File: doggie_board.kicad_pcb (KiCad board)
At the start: 2 copper layers, 127 x 127.5 mm, 86 parts, among them J1 XT90PW-M, J2 XT90PW-M, J5V1 Conn_01x02, J5V10 Conn_01x02, J5V11 Conn_01x02, J5V12 Conn_01x02, J5V13 Conn_01x02, J5V14 Conn_01x02, J5V15 Conn_01x02, J5V16 Conn_01x02, J5V17 Conn_01x02, J5V18 Conn_01x02, J5V19 Conn_01x02, J5V2 Conn_01x02, J5V20 Conn_01x02, J5V3 Conn_01x02, J5V4 Conn_01x02, J5V5 Conn_01x02, J5V6 Conn_01x02, J5V7 Conn_01x02, J5V8 Conn_01x02, J5V9 Conn_01x02, Q1 PSMN3R7-100BSEJ, Q2 PSMN3R7-100BSEJ, Q3 PSMN3R7-100BSEJ, Q4 PSMN3R7-100BSEJ, Q5 PSMN3R7-100BSEJ, Q6 PSMN3R7-100BSEJ, U1 TPS2490, U2 TPS2490, U3 LM76005, U4 LM76005, U5 LM76005

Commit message: progress on right drain
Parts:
- moved R5 9.63 mm to (127.1, 71.1), turned to -90 degrees
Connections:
- Q1 pad 2: (no net) -> /High Side Power Switch/drain_left
- Q2 pad 2: (no net) -> /High Side Power Switch/drain_left
- Q3 pad 2: (no net) -> /High Side Power Switch/drain_left
- Q4 pad 2: (no net) -> /High Side Power Switch/drain_r
- Q5 pad 2: (no net) -> /High Side Power Switch/drain_r
- Q6 pad 2: (no net) -> /High Side Power Switch/drain_r
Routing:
- net (no net): vias 1 -> 0
- added copper zone on F.Cu, net /High Side Power Switch/drain_left
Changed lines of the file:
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@@
 			(layers "F.Cu" "F.Mask")
 			(roundrect_rratio 0.026596)
+			(net 53 "/High Side Power Switch/drain_r")
+			(pintype "passive")
 		)
 		(pad "3" smd roundrect
@@
 			(layers "F.Cu" "F.Mask")
 			(roundrect_rratio 0.026596)
+			(net 53 "/High Side Power Switch/drain_r")
+			(pintype "passive")
 		)
 		(pad "3" smd roundrect
@@
 			(layers "F.Cu" "F.Mask")
 			(roundrect_rratio 0.026596)
+			(net 53 "/High Side Power Switch/drain_r")
+			(pintype "passive")
 		)
 		(pad "3" smd roundrect
@@
 			(layers "F.Cu" "F.Mask")
 			(roundrect_rratio 0.026596)
+			(net 51 "/High Side Power Switch/drain_left")
+			(pintype "passive")
 		)
 		(pad "3" smd roundrect
@@
 	(footprint "footprints:RES_PSR500_ROM"
 		(layer "F.Cu")
-		(at 130.25 62 180)
+		(at 127.1 71.1 -90)
 		(tags "PSR500HTQFC0L20 ")
 		(property "Reference" "R5"
-			(at 0 0 180)
+			(at 0 0 270)
 			(unlocked yes)
 			(layer "F.SilkS")
@@
 		)
 		(property "Value" "0.2m, 15W"
-			(at 0 0 180)
+			(at 0 0 270)
 			(unlocked yes)
 			(layer "F.Fab")
@@
 		)
 		(property "Datasheet" "~"
-			(at 0 0 180)
+			(at 0 0 90)
 			(layer "F.Fab")
 			(hide yes)
@@
 		)
 		(property "Description" "Resistor"
-			(at 0 0 180)
+			(at 0 0 90)
 			(layer "F.Fab")
 			(hide yes)
@@
 		)
 		(property "Sim.Device" ""
-			(at 0 0 180)
+			(at 0 0 270)
 			(unlocked yes)
 			(layer "F.Fab")
@@
 		)
 		(property "Sim.Pins" ""
-			(at 0 0 180)
+			(at 0 0 270)
 			(unlocked yes)
 			(layer "F.Fab")
@@
 		)
 		(property "Sim.Type" ""
-			(at 0 0 180)
+			(at 0 0 270)
 			(unlocked yes)
 			(layer "F.Fab")
@@
 		(attr smd)
 		(fp_line
-			(start 2.74045 -4.1529)
-			(end -2.74045 -4.1529)
+			(start -2.74045 4.1529)
+			(end 2.74045 4.1529)
 			(stroke
 				(width 0.1524)
@@
 		)
 		(fp_line
-			(start -2.74045 4.1529)
-			(end 2.74045 4.1529)
+			(start 2.74045 -4.1529)
+			(end -2.74045 -4.1529)
 			(stroke
 				(width 0.1524)
@@
 		)
 		(fp_line
-			(start 8.1026 4.2799)
-			(end -8.1026 4.2799)
+			(start -8.1026 4.2799)
+			(end -8.1026 -4.2799)
 			(stroke
 				(width 0.1524)
@@
 		)
 		(fp_line
-			(start 8.1026 -4.2799)
-			(end 8.1026 4.2799)
+			(start 8.1026 4.2799)
+			(end -8.1026 4.2799)
 			(stroke
 				(width 0.1524)
@@
 		)
 		(fp_line
-			(start -8.1026 4.2799)
-			(end -8.1026 -4.2799)
+			(start -8.1026 -4.2799)
+			(end 8.1026 -4.2799)
 			(stroke
 				(width 0.1524)
@@
 		)
 		(fp_line
-			(start -8.1026 -4.2799)
-			(end 8.1026 -4.2799)
+			(start 8.1026 -4.2799)
+			(end 8.1026 4.2799)
 			(stroke
 				(width 0.1524)
@@
 		)
 		(fp_line
-			(start 7.6454 4.0259)
-			(end 7.6454 -4.0259)
+			(start -7.6454 4.0259)
+			(end -3.048 4.0259)
 			(stroke
 				(width 0.0254)
@@
 		)
 		(fp_line
-			(start 7.6454 4.0259)
-			(end 7.6454 -4.0259)
+			(start -7.6454 4.0259)
+			(end 7.6454 4.0259)
 			(stroke
 				(width 0.0254)
@@
 		)
 		(fp_line
-			(start 7.6454 -4.0259)
-			(end 3.048 -4.0259)
+			(start -3.048 4.0259)
+			(end -3.048 -4.0259)
 			(stroke
 				(width 0.0254)
@@
 		)
 		(fp_line
-			(start 7.6454 -4.0259)
-			(end -7.6454 -4.0259)
+			(start 3.048 4.0259)
+			(end 7.6454 4.0259)
 			(stroke
 				(width 0.0254)
@@
 		)
 		(fp_line
-			(start 3.048 4.0259)
-			(end 7.6454 4.0259)
+			(start 7.6454 4.0259)
+			(end 7.6454 -4.0259)
 			(stroke
 				(width 0.0254)
@@
 		)
 		(fp_line
-			(start 3.048 -4.0259)
-			(end 3.048 4.0259)
+			(start 7.6454 4.0259)
+			(end 7.6454 -4.0259)
 			(stroke
 				(width 0.0254)
@@
 		)
 		(fp_line
-			(start -3.048 4.0259)
-			(end -3.048 -4.0259)
+			(start -7.6454 -4.0259)
+			(end -7.6454 4.0259)
 			(stroke
 				(width 0.0254)
@@
 		)
 		(fp_line
-			(start -3.048 -4.0259)
-			(end -7.6454 -4.0259)
+			(start -7.6454 -4.0259)
+			(end -7.6454 4.0259)
 			(stroke
 				(width 0.0254)
@@
 		)
 		(fp_line
-			(start -7.6454 4.0259)
-			(end 7.6454 4.0259)
+			(start -3.048 -4.0259)
+			(end -7.6454 -4.0259)
 			(stroke
 				(width 0.0254)
@@
 		)
 		(fp_line
-			(start -7.6454 4.0259)
-			(end -3.048 4.0259)
+			(start 3.048 -4.0259)
+			(end 3.048 4.0259)
 			(stroke
 				(width 0.0254)
@@
 		)
 		(fp_line
-			(start -7.6454 -4.0259)
-			(end -7.6454 4.0259)
+			(start 7.6454 -4.0259)
+			(end -7.6454 -4.0259)
 			(stroke
 				(width 0.0254)
@@
 		)
 		(fp_line
-			(start -7.6454 -4.0259)
-			(end -7.6454 4.0259)
+			(start 7.6454 -4.0259)
+			(end 3.048 -4.0259)
 			(stroke
 				(width 0.0254)
@@
 		)
 		(fp_text user "${REFERENCE}"
-			(at 0 0 180)
+			(at 0 0 270)
 			(unlocked yes)
 			(layer "F.Fab")
@@
 		)
 		(pad "1" smd rect
-			(at -5.4483 0 180)
+			(at -5.4483 0 270)
 			(size 4.8006 8.0518)
 			(layers "F.Cu" "F.Mask" "F.Paste")
@@
 		)
 		(pad "2" smd rect
-			(at 5.4483 0 180)
+			(at 5.4483 0 270)
 			(size 4.8006 8.0518)
 			(layers "F.Cu" "F.Mask" "F.Paste")
@@
 			(polygon
 				(pts
-					(xy 133.2472 65.9751) (xy 127.2528 65.9751) (xy 127.2528 58.0249) (xy 133.2472 58.0249)
+					(xy 131.0751 68.1028) (xy 131.0751 74.0972) (xy 123.1249 74.0972) (xy 123.1249 68.1028)
 				)
 			)
@@
 			(layers "F.Cu" "F.Mask")
 			(roundrect_rratio 0.026596)
+			(net 51 "/High Side Power Switch/drain_left")
+			(pintype "passive")
 		)
 		(pad "3" smd roundrect
@@
 			(layers "F.Cu" "F.Mask")
 			(roundrect_rratio 0.026596)
+			(net 51 "/High Side Power Switch/drain_left")
+			(pintype "passive")
 		)
 		(pad "3" smd roundrect
@@
 		(layer "Edge.Cuts")
 	)
-	(via
-		(at 131.4 126.45)
-		(size 1)
-		(drill 0.8)
-		(layers "F.Cu" "B.Cu")
-		(free yes)
-		(net 0)
-	)
 	(zone
 		(net 2)
@@
 			)
 		)
+	)
+	(zone
+		(net 51)
+		(net_name "/High Side Power Switch/drain_left")
+		(layer "F.Cu")
+		(hatch edge 0.5)
+		(priority 1)
+		(connect_pads
+			(clearance 0.5)
+		)
+		(min_thickness 0.25)
+		(filled_areas_thickness no)
+		(fill yes
+			(thermal_gap 0.5)
+			(thermal_bridge_width 0.5)
+		)
+		(polygon
+			(pts
+				(xy 120.2 71.7) (xy 119.8 162.7) (xy 133 162.7) (xy 133 71.7)
+			)
+		)

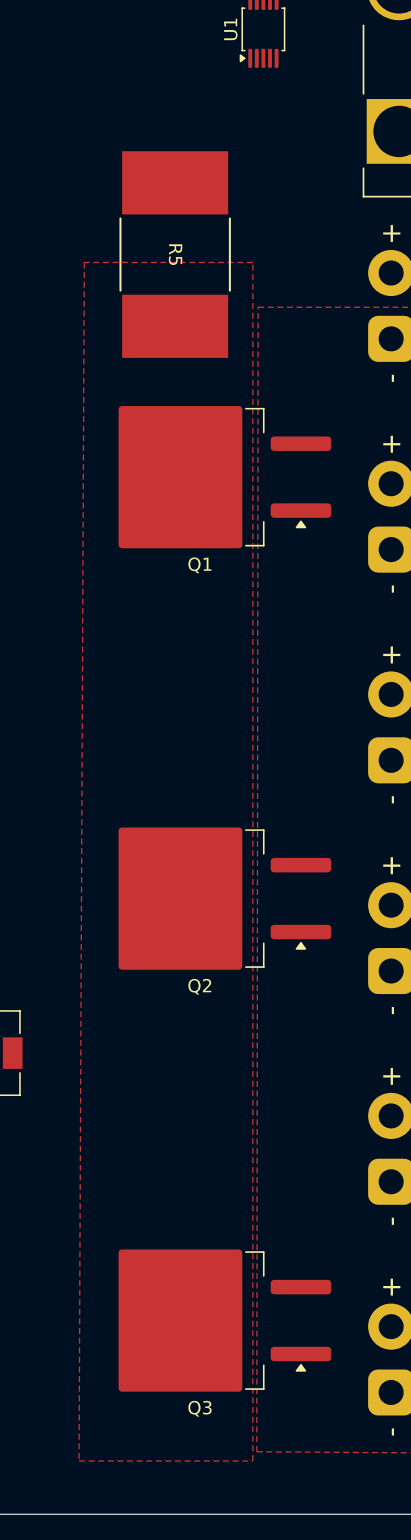
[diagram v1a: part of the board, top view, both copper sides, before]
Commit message: swapped left and right
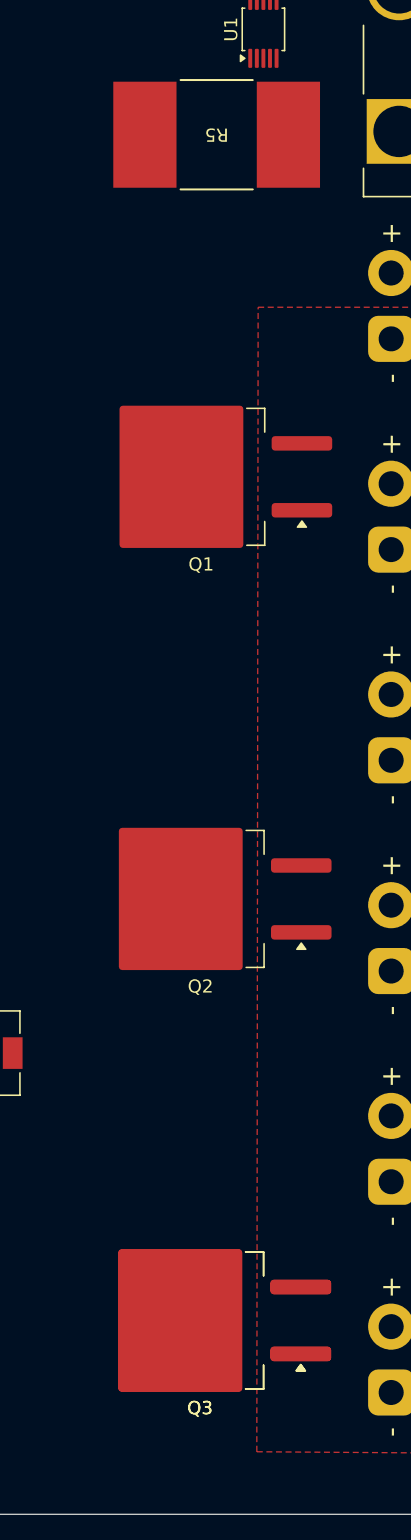
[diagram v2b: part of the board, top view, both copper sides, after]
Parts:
- added Q3: PSMN3R7-100BSEJ, Package_TO_SOT_SMD:TO-263-2, F.Cu at (129.0, 152.0)
- moved R5 9.63 mm to (130.2, 62.0), turned to 180 degrees
- moved Q1 0.08 mm to (129.1, 88.0)
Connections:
- Q3 pad 2: /High Side Power Switch/drain_left -> (no net)
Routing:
- removed copper zone on F.Cu, net /High Side Power Switch/drain_left

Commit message: Fixed Schematics with more cost effective IC's
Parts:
- removed the Q3 at (129.0, 152.0)
- added J3: Conn_01x02, Connector_PinHeader_2.54mm:PinHeader_1x02_P2.54mm_Vertical, F.Cu at (258.0, 124.5)
- C3: value 0.1uF, 100V -> 2.2uF
- C4: value 27nF, 100V -> 10nF
- R10: value 100k -> 50; footprint Resistor_SMD:R_0201_0603Metric_Pad0.64x0.40mm_HandSolder -> Resistor_SMD:R_1206_3216Metric_Pad1.30x1.75mm_HandSolder
- R11: value 18k -> 50; footprint Resistor_SMD:R_0201_0603Metric_Pad0.64x0.40mm_HandSolder -> Resistor_SMD:R_1206_3216Metric_Pad1.30x1.75mm_HandSolder
- R12: value 0.2m, 15W -> 50; footprint footprints:RES_PSR500_ROM -> Resistor_SMD:R_1206_3216Metric_Pad1.30x1.75mm_HandSolder
- R13: value 50 -> 200k
- R14: value 50 -> 100k
- R15: value 50 -> 560
- R16: value 1k -> 2.2
- U4: value LM76005 -> MIC28516T-E/PHA
- moved C1 86.6 mm to (135.0, 45.0), turned to 90 degrees
- moved R1 82.7 mm to (132.5, 60.0)
- moved R2 58.1 mm to (129.0, 60.0)
- moved U1 18.9 mm to (115.2, 57.1)
- moved R5 9.41 mm to (127.5, 71.0), turned to -90 degrees
- moved D1 2.92 mm to (127.0, 47.2), turned to 180 degrees
- moved J1 2.65 mm to (150.8, 56.3)
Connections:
- C1 pad 1: 48_L -> 48_RAW
- C3 pad 1: 48_R -> /12v Buck Converter/VDD
- C4 pad 1: Net-(C4-Pad1) -> /12v Buck Converter/BST
- C4 pad 2: GND -> Net-(C4-Pad2)
- Cboot2 pad 1: Net-(U4-BOOT) -> unconnected-(Cboot2-Pad1)
- Cin1 pad 1: +48V -> 48_R
- Cin2 pad 1: +48V -> 48_R
- Cinx1 pad 1: +48V -> 48_R
- Cinx2 pad 1: +48V -> 48_R
- Cinx3 pad 1: +48V -> 48_R
- Cvcc2 pad 1: Net-(U4-VCC) -> unconnected-(Cvcc2-Pad1)
- D1 pad 1: 48_L -> 48_RAW
- D2 pad 1: 48_R -> 48_L
- J1 pad P: 48_L -> 48_RAW
- J2 pad P: 48_R -> 48_RAW
- Q1 pad 2: /High Side Power Switch/drain_left -> /High Side Power Switch/drain_R
- Q2 pad 2: /High Side Power Switch/drain_left -> /High Side Power Switch/drain_R
- Q3 pad 2: /High Side Power Switch/drain_left -> /High Side Power Switch/drain_R
- Q4 pad 2: /High Side Power Switch/drain_r -> /High Side Power Switch/drain_R
- Q5 pad 2: /High Side Power Switch/drain_r -> /High Side Power Switch/drain_R
- Q6 pad 2: /High Side Power Switch/drain_r -> /High Side Power Switch/drain_R
- R1 pad 1: 48_L -> 48_RAW
- R10 pad 1: Net-(U2-VREF) -> /High Side Power Switch/gate_line_R
- R10 pad 2: Net-(U2-PROG) -> Net-(Q4-Pad1)
- R11 pad 1: Net-(U2-PROG) -> /High Side Power Switch/gate_line_R
- R11 pad 2: GND -> Net-(Q5-Pad1)
- R12 pad 1: 48_R -> /High Side Power Switch/gate_line_R
- R12 pad 2: /High Side Power Switch/drain_r -> Net-(Q6-Pad1)
- R13 pad 1: /High Side Power Switch/gate_line_r -> 48_RAW
- R13 pad 2: Net-(Q4-Pad1) -> /12v Buck Converter/FREQ
- R14 pad 1: /High Side Power Switch/gate_line_r -> GND
- R14 pad 2: Net-(Q5-Pad1) -> /12v Buck Converter/FREQ
- R15 pad 1: /High Side Power Switch/gate_line_r -> /12v Buck Converter/FB
- R15 pad 2: Net-(Q6-Pad1) -> Net-(C4-Pad2)
- R16 pad 1: Net-(C4-Pad1) -> 48_RAW
- R16 pad 2: /High Side Power Switch/gate_line_r -> /12v Buck Converter/SVIN
- R5 pad 1: 48_L -> 48_RAW
- R5 pad 2: /High Side Power Switch/drain_left -> /High Side Power Switch/drain_R
- R6 pad 1: /High Side Power Switch/gate_line_left -> /High Side Power Switch/gate_line_R
- R7 pad 1: /High Side Power Switch/gate_line_left -> /High Side Power Switch/gate_line_R
- R8 pad 1: /High Side Power Switch/gate_line_left -> /High Side Power Switch/gate_line_R
- R9 pad 2: /High Side Power Switch/gate_line_left -> /High Side Power Switch/gate_line_R
- Rfbb2 pad 1: Net-(U4-FB) -> Net-(Rfbb2-Pad1)
- Rfbt2 pad 2: Net-(U4-FB) -> Net-(Rfbb2-Pad1)
- Rpgood2 pad 1: Net-(U4-PGOOD) -> unconnected-(Rpgood2-Pad1)
- U1 pad 10: 48_L -> 48_RAW
- U1 pad 6: unconnected-(U1-PG-Pad6) -> 48V_PG
- U1 pad 8: /High Side Power Switch/gate_line_left -> /High Side Power Switch/gate_line_R
- U1 pad 9: /High Side Power Switch/drain_left -> /High Side Power Switch/drain_R
- U2 pad 10: 48_R -> 48_L
- U2 pad 8: /High Side Power Switch/gate_line_r -> /High Side Power Switch/gate_line_L
- U2 pad 9: /High Side Power Switch/drain_r -> /High Side Power Switch/drain_L
- U3 pad 18: +48V -> 48_R
- U3 pad 20: +48V -> 48_R
- U3 pad 21: +48V -> 48_R
- U3 pad 22: +48V -> 48_R
- U4 pad 1: Net-(Cboot2-Pad2) -> /12v Buck Converter/ILIM
- U4 pad 10: GND -> 48_RAW
- U4 pad 11: GND -> 48_RAW
- U4 pad 12: Net-(U4-FB) -> /12v Buck Converter/SW
- U4 pad 13: GND -> /12v Buck Converter/SW
- U4 pad 14: GND -> /12v Buck Converter/SW
- U4 pad 15: GND -> /12v Buck Converter/SW
- U4 pad 16: Net-(U4-PGOOD) -> GND
- U4 pad 18: +48V -> GND
- U4 pad 2: Net-(Cboot2-Pad2) -> GND
- U4 pad 20: +48V -> /12v Buck Converter/SW
- U4 pad 21: +48V -> /12v Buck Converter/PVDD
- U4 pad 22: +48V -> GND
- U4 pad 23: unconnected-(U4-NC-Pad23) -> GND
- U4 pad 24: GND -> 48_RAW
- U4 pad 25: GND -> /12v Buck Converter/FREQ
- U4 pad 26: GND -> Net-(U4-SS)
- U4 pad 27: GND -> /12v Buck Converter/FB
- U4 pad 3: Net-(Cboot2-Pad2) -> /12v Buck Converter/SW
- U4 pad 30: GND -> /12v Buck Converter/VDD
- U4 pad 31: GND -> /12v Buck Converter/SVIN
- U4 pad 4: Net-(Cboot2-Pad2) -> /12v Buck Converter/BST
- U4 pad 5: Net-(Cboot2-Pad2) -> 48_RAW
- U4 pad 6: Net-(U4-BOOT) -> 48_RAW
- U4 pad 7: unconnected-(U4-NC-Pad7) -> 48_RAW
- U4 pad 8: Net-(U4-VCC) -> 48_RAW
- U4 pad 9: GND -> 48_RAW
- U5 pad 18: +48V -> 48_R
- U5 pad 20: +48V -> 48_R
- U5 pad 21: +48V -> 48_R
- U5 pad 22: +48V -> 48_R

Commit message: feat: added footprints
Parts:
- added C10: 10u, Capacitor_SMD:C_0201_0603Metric_Pad0.64x0.40mm_HandSolder, F.Cu at (245.9, 52.0)
- added C11: 10u, Capacitor_SMD:C_0201_0603Metric_Pad0.64x0.40mm_HandSolder, F.Cu at (245.9, 53.8)
- added C12: 100n, Capacitor_SMD:C_0201_0603Metric_Pad0.64x0.40mm_HandSolder, F.Cu at (245.9, 55.5)
- added C13: 33p, Capacitor_SMD:C_0201_0603Metric_Pad0.64x0.40mm_HandSolder, F.Cu at (245.9, 57.2)
- added C14: 22u, Capacitor_SMD:C_0201_0603Metric_Pad0.64x0.40mm_HandSolder, F.Cu at (245.9, 59.0)
- added C15: 22u, Capacitor_SMD:C_0201_0603Metric_Pad0.64x0.40mm_HandSolder, F.Cu at (248.8, 52.0)
- added C16: 22u, Capacitor_SMD:C_0201_0603Metric_Pad0.64x0.40mm_HandSolder, F.Cu at (248.8, 53.8)
- added C17: 22u, Capacitor_SMD:C_0201_0603Metric_Pad0.64x0.40mm_HandSolder, F.Cu at (248.8, 55.5)
- added C18: 100n, Capacitor_SMD:C_0201_0603Metric_Pad0.64x0.40mm_HandSolder, F.Cu at (248.8, 57.2)
- added C19: 10u, Capacitor_SMD:C_0201_0603Metric_Pad0.64x0.40mm_HandSolder, F.Cu at (245.9, 62.8)
- added C20: 10u, Capacitor_SMD:C_0201_0603Metric_Pad0.64x0.40mm_HandSolder, F.Cu at (245.9, 64.5)
- added C21: 100n, Capacitor_SMD:C_0201_0603Metric_Pad0.64x0.40mm_HandSolder, F.Cu at (245.9, 66.2)
- added C22: 56p, Capacitor_SMD:C_0201_0603Metric_Pad0.64x0.40mm_HandSolder, F.Cu at (245.9, 68.0)
- added C23: 22u, Capacitor_SMD:C_0201_0603Metric_Pad0.64x0.40mm_HandSolder, F.Cu at (245.9, 69.8)
- added C24: 22u, Capacitor_SMD:C_0201_0603Metric_Pad0.64x0.40mm_HandSolder, F.Cu at (248.8, 62.8)
- added C25: 22u, Capacitor_SMD:C_0201_0603Metric_Pad0.64x0.40mm_HandSolder, F.Cu at (248.8, 64.5)
- added C26: 22u, Capacitor_SMD:C_0201_0603Metric_Pad0.64x0.40mm_HandSolder, F.Cu at (248.8, 66.2)
- added C27: 100n, Capacitor_SMD:C_0201_0603Metric_Pad0.64x0.40mm_HandSolder, F.Cu at (248.8, 68.0)
- added C5: 1.8n, Capacitor_SMD:C_0201_0603Metric_Pad0.64x0.40mm_HandSolder, F.Cu at (245.9, 39.5)
- added C6: 2.2u, Capacitor_SMD:C_0201_0603Metric_Pad0.64x0.40mm_HandSolder, F.Cu at (245.9, 41.2)
- added C7: 47p, Capacitor_SMD:C_0201_0603Metric_Pad0.64x0.40mm_HandSolder, F.Cu at (245.9, 43.0)
- added C8: 2.2u, Capacitor_SMD:C_0201_0603Metric_Pad0.64x0.40mm_HandSolder, F.Cu at (245.9, 44.8)
- added C9: 10u, Capacitor_SMD:C_0201_0603Metric_Pad0.64x0.40mm_HandSolder, F.Cu at (245.9, 46.5)
- added H1: MountingHole_Pad, MountingHole:MountingHole_5.3mm_M5_DIN965_Pad_TopBottom, F.Cu at (237.2, 44.0)
- added H2: MountingHole_Pad, MountingHole:MountingHole_5.3mm_M5_DIN965_Pad_TopBottom, F.Cu at (237.2, 54.8)
- added H3: MountingHole_Pad, MountingHole:MountingHole_5.3mm_M5_DIN965_Pad_TopBottom, F.Cu at (237.2, 65.5)
- added H4: MountingHole_Pad, MountingHole:MountingHole_5.3mm_M5_DIN965_Pad_TopBottom, F.Cu at (237.2, 76.2)
- added J5V21: Conn_01x02, Connector_BarrelJack:BarrelJack_CUI_PJ-079BH_Horizontal, F.Cu at (173.4, 114.9)
- added J5V22: Conn_01x02, Connector_PinHeader_1.00mm:PinHeader_1x02_P1.00mm_Vertical, F.Cu at (163.8, 127.8)
- added J5V23: Conn_01x02, Connector_PinHeader_1.00mm:PinHeader_1x02_P1.00mm_Vertical, F.Cu at (167.2, 127.8)
- added J5V24: Conn_01x02, Connector_PinHeader_1.00mm:PinHeader_1x02_P1.00mm_Vertical, F.Cu at (170.5, 127.8)
- added L3: 2.2u, Capacitor_SMD:C_0201_0603Metric_Pad0.64x0.40mm_HandSolder, F.Cu at (248.8, 69.8)
- added R17: 4.42k, Resistor_SMD:R_0201_0603Metric_Pad0.64x0.40mm_HandSolder, F.Cu at (245.9, 48.2)
- added R19: 100k, Resistor_SMD:R_0201_0603Metric_Pad0.64x0.40mm_HandSolder, F.Cu at (248.8, 59.0)
- added R20: 20k, Resistor_SMD:R_0201_0603Metric_Pad0.64x0.40mm_HandSolder, F.Cu at (251.6, 52.0)
- added R21: 220k, Resistor_SMD:R_0201_0603Metric_Pad0.64x0.40mm_HandSolder, F.Cu at (251.6, 53.8)
- added R22: 30k, Resistor_SMD:R_0201_0603Metric_Pad0.64x0.40mm_HandSolder, F.Cu at (251.6, 55.5)
- added R23: 100k, Resistor_SMD:R_0201_0603Metric_Pad0.64x0.40mm_HandSolder, F.Cu at (251.6, 62.8)
- added R24: 20k, Resistor_SMD:R_0201_0603Metric_Pad0.64x0.40mm_HandSolder, F.Cu at (251.6, 64.5)
- added R25: 135k, Resistor_SMD:R_0201_0603Metric_Pad0.64x0.40mm_HandSolder, F.Cu at (251.6, 66.2)
- added R26: 30k, Resistor_SMD:R_0201_0603Metric_Pad0.64x0.40mm_HandSolder, F.Cu at (251.6, 68.0)
- C1: value 0.1uF, 100V -> 0.1u, 100V; footprint Capacitor_SMD:C_1206_3216Metric_Pad1.33x1.80mm_HandSolder -> Capacitor_SMD:C_0201_0603Metric_Pad0.64x0.40mm_HandSolder
- C2: value 27nF, 100V -> 27n, 100V; footprint Capacitor_SMD:C_1206_3216Metric_Pad1.33x1.80mm_HandSolder -> Capacitor_SMD:C_0201_0603Metric_Pad0.64x0.40mm_HandSolder
- C3: value 2.2uF -> 2.2u; footprint Capacitor_SMD:C_1206_3216Metric_Pad1.33x1.80mm_HandSolder -> Capacitor_SMD:C_0201_0603Metric_Pad0.64x0.40mm_HandSolder
- C4: value 10nF -> 2.2u; footprint Capacitor_SMD:C_1206_3216Metric_Pad1.33x1.80mm_HandSolder -> Capacitor_SMD:C_0201_0603Metric_Pad0.64x0.40mm_HandSolder
- Ct1: value 1nF -> 1n; footprint Capacitor_SMD:C_0805_2012Metric_Pad1.18x1.45mm_HandSolder -> Capacitor_SMD:C_0201_0603Metric_Pad0.64x0.40mm_HandSolder
- J1: value XT90PW-M -> Conn_01x02; footprint footprints:AMASS_XT90PW-M -> Connector_PinHeader_2.54mm:PinHeader_1x02_P2.54mm_Vertical
- J3: value Conn_01x02 -> XT90PW-M; footprint Connector_PinHeader_2.54mm:PinHeader_1x02_P2.54mm_Vertical -> footprints:AMASS_XT90PW-M
- J5V13: footprint Connector_PinHeader_1.00mm:PinHeader_1x02_P1.00mm_Vertical -> Connector_BarrelJack:BarrelJack_CUI_PJ-079BH_Horizontal
- L1: value 15uH, 16.9mOhm -> 4.7u
- L2: value 5.6uH -> 2.2u; footprint Inductor_SMD:L_6.3x6.3_H3 -> Capacitor_SMD:C_0201_0603Metric_Pad0.64x0.40mm_HandSolder
- Q1, Q2, Q3, Q4, Q5, Q6: footprint Package_TO_SOT_SMD:TO-263-2 -> footprints:D2PAK_NEX
- R10, R11, R6, R7, R8: value 50 -> 60; footprint Resistor_SMD:R_1206_3216Metric_Pad1.30x1.75mm_HandSolder -> Resistor_SMD:R_0201_0603Metric_Pad0.64x0.40mm_HandSolder
- R12: value 50 -> 1k; footprint Resistor_SMD:R_1206_3216Metric_Pad1.30x1.75mm_HandSolder -> Resistor_SMD:R_0201_0603Metric_Pad0.64x0.40mm_HandSolder
- R13: value 200k -> 24.9k; footprint Resistor_SMD:R_1206_3216Metric_Pad1.30x1.75mm_HandSolder -> Resistor_SMD:R_0201_0603Metric_Pad0.64x0.40mm_HandSolder
- R14: value 100k -> 40.2k; footprint Resistor_SMD:R_1206_3216Metric_Pad1.30x1.75mm_HandSolder -> Resistor_SMD:R_0201_0603Metric_Pad0.64x0.40mm_HandSolder
- R15: value 560 -> 100k; footprint Resistor_SMD:R_1206_3216Metric_Pad1.30x1.75mm_HandSolder -> Resistor_SMD:R_0201_0603Metric_Pad0.64x0.40mm_HandSolder
- R16: value 2.2 -> 47.5k; footprint Resistor_SMD:R_1206_3216Metric_Pad1.30x1.75mm_HandSolder -> Resistor_SMD:R_0201_0603Metric_Pad0.64x0.40mm_HandSolder
- R9: value 1k -> 60; footprint Resistor_SMD:R_1206_3216Metric_Pad1.30x1.75mm_HandSolder -> Resistor_SMD:R_0201_0603Metric_Pad0.64x0.40mm_HandSolder
- U2: value TPS2490 -> LM5148RGYR; footprint Package_SO:VSSOP-10_3x3mm_P0.5mm -> footprints:QFN50P550X350X100-25N
- U3: value LM76005 -> TPS566242DRLR; footprint Package_DFN_QFN:Texas_RNP0030B_WQFN-30-1EP_4x6mm_P0.5mm_EP1.8x4.5mm_ThermalVias -> footprints:SOT5x3_DRL_TEX
- U4: value MIC28516T-E/PHA -> TPS566242DRLR; footprint Package_DFN_QFN:Texas_RNP0030B_WQFN-30-1EP_4x6mm_P0.5mm_EP1.8x4.5mm -> footprints:SOT5x3_DRL_TEX
- moved R14 149.4 mm to (202.2, 68.2)
- moved J3 129.8 mm to (151.2, 50.5), turned to 90 degrees
- moved L1 125.9 mm to (237.1, 117.2)
- moved Rfbb1 125.9 mm to (229.3, 125.5)
- moved Rfbt1 125.9 mm to (229.3, 127.3)
- moved Rpgood1 125.9 mm to (229.3, 129.0)
- moved Rpgood2 125.9 mm to (229.3, 109.0)
- moved U4 125.9 mm to (220.1, 141.0)
- moved R12 112.5 mm to (184.1, 27.5)
- moved U2 112.5 mm to (170.6, 32.1)
- moved C1 88.6 mm to (220.2, 21.0)
- moved J1 88.6 mm to (236.1, 32.3)
- moved R1 88.6 mm to (217.8, 36.0)
- moved R2 88.6 mm to (214.2, 36.0)
- moved L2 85.1 mm to (140.9, 184.8)
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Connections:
- net /High Side Power Switch/drain_R renamed /High Side Power Switch/drain_line
- C3 pad 1: /12v Buck Converter/VDD -> 48_RAW
- C4 pad 1: /12v Buck Converter/BST -> Net-(U2-CBOOT)
- C4 pad 2: Net-(C4-Pad2) -> Net-(U2-SW)
- J5V13 pad 1: +3.3V -> +12V
- J5V14 pad 1: +3.3V -> +12V
- J5V15 pad 1: +3.3V -> +12V
- J5V16 pad 1: +3.3V -> +12V
- J5V17 pad 1: +5V -> +3.3V
- J5V18 pad 1: +5V -> +3.3V
- J5V19 pad 1: +5V -> +3.3V
- J5V20 pad 1: +5V -> +3.3V
- L1 pad 1: Net-(Cboot1-Pad2) -> Net-(U2-SW)
- L1 pad 2: +12V -> Net-(U2-ISNS+)
- L2 pad 1: Net-(Cboot2-Pad2) -> /5v Buck Converter/SW
- R1 pad 2: Net-(J3-Pin_1) -> /High Side Power Switch/sw_low
- R10 pad 1: /High Side Power Switch/gate_line_R -> /High Side Power Switch/gate_line
- R10 pad 2: Net-(Q4-Pad1) -> Net-(Q5-Pad1)
- R11 pad 1: /High Side Power Switch/gate_line_R -> /High Side Power Switch/gate_line
- R11 pad 2: Net-(Q5-Pad1) -> Net-(Q6-Pad1)
- R12 pad 1: /High Side Power Switch/gate_line_R -> Net-(C2-Pad1)
- R12 pad 2: Net-(Q6-Pad1) -> /High Side Power Switch/gate_line
- R13 pad 1: 48_RAW -> /12v Buck Converter/RT
- R13 pad 2: /12v Buck Converter/FREQ -> GND
- R14 pad 1: GND -> Net-(U2-CNFG)
- R14 pad 2: /12v Buck Converter/FREQ -> GND
- R15 pad 1: /12v Buck Converter/FB -> /12v Buck Converter/VCC
- R15 pad 2: Net-(C4-Pad2) -> Net-(U2-PG/SYNCOUT)
- R16 pad 1: 48_RAW -> /12v Buck Converter/PFM_SYNC
- R16 pad 2: /12v Buck Converter/SVIN -> Net-(U2-FB)
- R2 pad 1: Net-(J3-Pin_1) -> /High Side Power Switch/sw_low
- R6 pad 1: /High Side Power Switch/gate_line_R -> /High Side Power Switch/gate_line
- R7 pad 1: /High Side Power Switch/gate_line_R -> /High Side Power Switch/gate_line
- R8 pad 1: /High Side Power Switch/gate_line_R -> /High Side Power Switch/gate_line
- R9 pad 1: Net-(C2-Pad1) -> /High Side Power Switch/gate_line
- R9 pad 2: /High Side Power Switch/gate_line_R -> Net-(Q4-Pad1)
- U1 pad 8: /High Side Power Switch/gate_line_R -> /High Side Power Switch/gate_line
- U2 pad 1: ps_sw -> unconnected-(U2-NC-Pad1)
- U2 pad 10: 48_L -> GND
- U2 pad 2: Net-(U2-VREF) -> unconnected-(U2-NC__1-Pad2)
- U2 pad 3: Net-(U2-PROG) -> Net-(U2-CNFG)
- U2 pad 4: Net-(U2-TIMER) -> /12v Buck Converter/RT
- U2 pad 5: GND -> Net-(U2-EXTCOMP)
- U2 pad 6: unconnected-(U2-PG-Pad6) -> Net-(U2-FB)
- U2 pad 7: +48V -> GND
- U2 pad 8: /High Side Power Switch/gate_line_L -> /12v Buck Converter/PFM_SYNC
- U2 pad 9: /High Side Power Switch/drain_L -> /12v Buck Converter/VCC
- U3 pad 1: Net-(Cboot1-Pad2) -> +12V
- U3 pad 2: Net-(Cboot1-Pad2) -> /5v Buck Converter/SW
- U3 pad 3: Net-(Cboot1-Pad2) -> GND
- U3 pad 4: Net-(Cboot1-Pad2) -> GND
- U3 pad 5: Net-(Cboot1-Pad2) -> /5v Buck Converter/EN
- U3 pad 6: Net-(U3-BOOT) -> Net-(U3-FB)
- U4 pad 1: /12v Buck Converter/ILIM -> +12V
- U4 pad 2: GND -> /3.3v Buck Converter/SW
- U4 pad 3: /12v Buck Converter/SW -> GND
- U4 pad 4: /12v Buck Converter/BST -> GND
- U4 pad 5: 48_RAW -> /3.3v Buck Converter/EN
- U4 pad 6: 48_RAW -> Net-(U4-FB)
